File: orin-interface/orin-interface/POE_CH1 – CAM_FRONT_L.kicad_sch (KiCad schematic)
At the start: 1 part, among them J2 653108124022

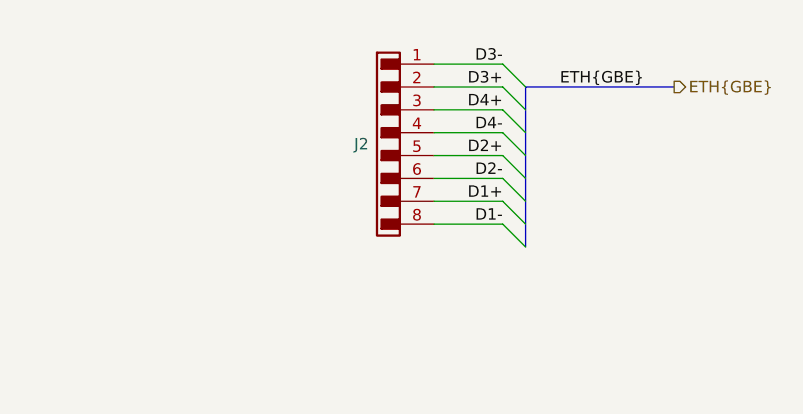
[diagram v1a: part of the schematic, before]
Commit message: orin-interface: add ETH connector sheets and Mate-connectors footprint lib; update orin-bob
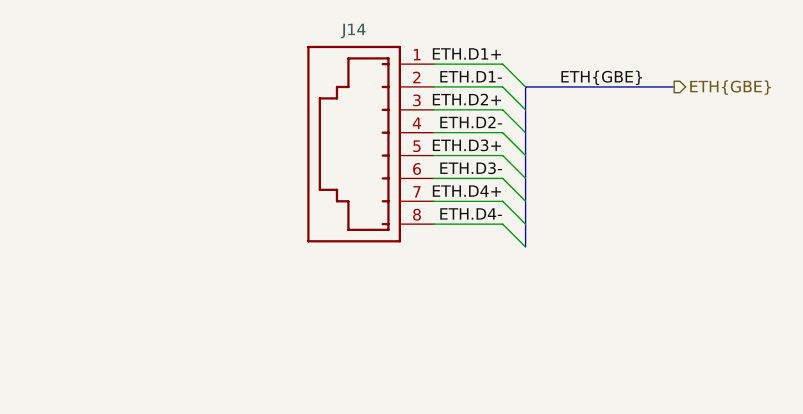
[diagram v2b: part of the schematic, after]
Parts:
- removed J2: 653108124022, Connector_SMD_Wurth:J_Wurth_WR-WTB_653108124022, symbol Wurth_WR-WTB:653108124022
- added J14: 634008138121, 615008138021:J_Wurth_WR-MJ_634008138121, symbol WR-MJ:634008138121
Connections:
- new net ETH.D1+: J14.1
- new net ETH.D1-: J14.2
- new net ETH.D2+: J14.3
- new net ETH.D2-: J14.4
- new net ETH.D3+: J14.5
- new net ETH.D3-: J14.6
- new net ETH.D4+: J14.7
- new net ETH.D4-: J14.8
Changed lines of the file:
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@@
 	(wire
 		(pts
-			(xy 172.72 99.06) (xy 165.1 99.06)
+			(xy 165.1 106.68) (xy 172.72 106.68)
 		)
 		(stroke
@@
 	(wire
 		(pts
-			(xy 172.72 96.52) (xy 165.1 96.52)
+			(xy 165.1 93.98) (xy 172.72 93.98)
 		)
 		(stroke
@@
 		)
 	)
-	(wire
+	(bus
 		(pts
-			(xy 172.72 104.14) (xy 165.1 104.14)
+			(xy 175.26 91.44) (xy 175.26 109.22)
 		)
 		(stroke
@@
 		)
 	)
-	(bus
+	(wire
 		(pts
-			(xy 175.26 91.44) (xy 175.26 109.22)
+			(xy 165.1 96.52) (xy 172.72 96.52)
 		)
 		(stroke
@@
 	(wire
 		(pts
-			(xy 172.72 88.9) (xy 165.1 88.9)
+			(xy 165.1 101.6) (xy 172.72 101.6)
 		)
 		(stroke
@@
 	(wire
 		(pts
-			(xy 172.72 91.44) (xy 165.1 91.44)
+			(xy 165.1 104.14) (xy 172.72 104.14)
 		)
 		(stroke
@@
 	(wire
 		(pts
-			(xy 172.72 101.6) (xy 165.1 101.6)
+			(xy 165.1 99.06) (xy 172.72 99.06)
 		)
 		(stroke
@@
 	(wire
 		(pts
-			(xy 172.72 106.68) (xy 165.1 106.68)
+			(xy 165.1 91.44) (xy 172.72 91.44)
 		)
 		(stroke
@@
 	(wire
 		(pts
-			(xy 172.72 93.98) (xy 165.1 93.98)
+			(xy 165.1 88.9) (xy 172.72 88.9)
 		)
 		(stroke
@@
 		)
 	)
-	(label "D3+"
-		(at 172.72 91.44 180)
+	(label "ETH.D3+"
+		(at 172.72 99.06 180)
 		(effects
 			(font
@@
 		)
 	)
-	(label "D2+"
-		(at 172.72 99.06 180)
+	(label "ETH.D2+"
+		(at 172.72 93.98 180)
 		(effects
 			(font
@@
 		)
 	)
-	(label "D3-"
-		(at 172.72 88.9 180)
+	(label "ETH.D3-"
+		(at 172.72 101.6 180)
 		(effects
 			(font
@@
 		)
 	)
-	(label "D4-"
-		(at 172.72 96.52 180)
+	(label "ETH.D4-"
+		(at 172.72 106.68 180)
 		(effects
 			(font
@@
 		)
 	)
-	(label "D1+"
-		(at 172.72 104.14 180)
+	(label "ETH.D1+"
+		(at 172.72 88.9 180)
 		(effects
 			(font
@@
 		)
 	)
-	(label "D2-"
-		(at 172.72 101.6 180)
+	(label "ETH.D2-"
+		(at 172.72 96.52 180)
 		(effects
 			(font
@@
 		)
 	)
-	(label "D1-"
-		(at 172.72 106.68 180)
+	(label "ETH.D1-"
+		(at 172.72 91.44 180)
 		(effects
 			(font
@@
 		)
 	)
-	(label "D4+"
-		(at 172.72 93.98 180)
+	(label "ETH.D4+"
+		(at 172.72 104.14 180)
 		(effects
 			(font
@@
 	)
 	(symbol
-		(lib_id "Wurth_WR-WTB:653108124022")
-		(at 160.02 97.79 90)
-		(mirror x)
+		(lib_id "WR-MJ:634008138121")
+		(at 156.21 96.52 90)
 		(unit 1)
 		(body_style 1)
@@
 		(in_pos_files yes)
 		(dnp no)
-		(property "Reference" "J2"
-			(at 156.21 97.79 90)
+		(fields_autoplaced yes)
+		(property "Reference" "J14"
+			(at 156.21 85.09 90)
 			(show_name no)
 			(do_not_autoplace no)
@@
 					(size 1.27 1.27)
 				)
-				(justify right)
 			)
 		)
-		(property "Value" "653108124022"
-			(at 172.72 97.79 0)
+		(property "Value" "634008138121"
+			(at 172.72 96.52 0)
 			(hide yes)
 			(show_name no)
@@
 			)
 		)
-		(property "Footprint" "Connector_SMD_Wurth:J_Wurth_WR-WTB_653108124022"
-			(at 152.4 97.79 0)
+		(property "Footprint" "615008138021:J_Wurth_WR-MJ_634008138121"
+			(at 143.51 96.52 0)
 			(hide yes)
 			(show_name no)
@@
 			)
 		)
-		(property "Datasheet" "https://www.we-online.com/en/components/products/datasheet/653108124022?ki"
-			(at 142.24 143.51 0)
+		(property "Datasheet" "https://www.we-online.com/en/components/products/datasheet/634008138121?ki"
+			(at 148.59 33.02 0)
 			(hide yes)
 			(show_name no)
@@
 			)
 		)
-		(property "Description" "1.25 mm SMT Male Vertical Shrouded Header"
-			(at 160.02 97.79 0)
+		(property "Description" "Modular Jack SMT Vertical Plastic 8P8C"
+			(at 156.21 96.52 0)
 			(hide yes)
 			(show_name no)
@@
 		)
 		(property "Manufacturer" "Wurth Elektronik"
-			(at 144.78 143.51 0)
+			(at 151.13 33.02 0)
 			(hide yes)
 			(show_name no)
@@
 		)
 		(property "Manufacturer URL" "https://www.we-online.com"
-			(at 147.32 143.51 0)
-			(hide yes)
-			(show_name no)
-			(do_not_autoplace no)
-			(effects
-				(font
-					(size 1.27 1.27)
-				)
-			)
-		)
-		(property "Series" "WR-WTB"
-			(at 149.86 143.51 0)
-			(hide yes)
-			(show_name no)
-			(do_not_autoplace no)
-			(effects
-				(font
-					(size 1.27 1.27)
-				)
-			)
-		)
-		(property "Pins (pcs)" "8"
-			(at 152.4 143.51 0)
+			(at 153.67 33.02 0)
 			(hide yes)
 			(show_name no)
@@
 			)
 		)
-		(property "Pitch (mm)" "1.25"
-			(at 154.94 143.51 0)
+		(property "Series" "WR-MJ"
+			(at 156.21 33.02 0)
 			(hide yes)
 			(show_name no)
@@
 			)
 		)
-		(property "Gender" "Male"
-			(at 157.48 143.51 0)
+		(property "xPxC" "8P8C"
+			(at 158.75 33.02 0)
 			(hide yes)
 			(show_name no)
@@
 			)
 		)
-		(property "Type" "Vertical"
-			(at 160.02 143.51 0)
+		(property "EMI" "No"
+			(at 161.29 33.02 0)
 			(hide yes)
 			(show_name no)
@@
 			)
 		)
-		(property "Mounting Technology" "SMT"
-			(at 162.56 143.51 0)
+		(property "Mount" "SMT"
+			(at 163.83 33.02 0)
 			(hide yes)
 			(show_name no)
@@
 			)
 		)
-		(property "IR (A)" "1"
-			(at 165.1 143.51 0)
-			(hide yes)
-			(show_name no)
-			(do_not_autoplace no)
-			(effects
-				(font
-					(size 1.27 1.27)
-				)
-			)
-		)
-		(property "Working Voltage (V (AC))" "125"
-			(at 167.64 143.51 0)
-			(hide yes)
-			(show_name no)
-			(do_not_autoplace no)
-			(effects
-				(font
-					(size 1.27 1.27)
-				)
-			)
-		)
-		(property "PCB/Cable/Panel" "PCB"
-			(at 170.18 143.51 0)
-			(hide yes)
-			(show_name no)
-			(do_not_autoplace no)
-			(effects
-				(font
-					(size 1.27 1.27)
-				)
-			)
-		)
-		(property "Contact Resistance (mohm)" "20"
-			(at 172.72 143.51 0)
-			(hide yes)
-			(show_name no)
-			(do_not_autoplace no)
-			(effects
-				(font
-					(size 1.27 1.27)
-				)
-			)
-		)
-		(property "Tol. R" "max."
-			(at 175.26 143.51 0)
-			(hide yes)
-			(show_name no)
-			(do_not_autoplace no)
-			(effects
-				(font
-					(size 1.27 1.27)
-				)
-			)
-		)
-		(property "L (mm)" "14.75"
-			(at 177.8 143.51 0)
+		(property "Application System" "CAT 3"
+			(at 166.37 33.02 0)
 			(hide yes)
 			(show_name no)
@@
 		(pin "3"
 		)
-		(pin "4"
+		(pin "1"
 		)
 		(pin "2"
 		)
-		(pin "5"
+		(pin "4"
 		)
-		(pin "6"
+		(pin "8"
 		)
-		(pin "1"
+		(pin "6"
 		)
-		(pin "8"
+		(pin "5"
 		)
 		(pin "7"
@@
 			(project "orin-interface"
 				(path "/18aef7c7-2f0e-4a2c-9e5d-7b655e80b6a3/25e0c24f-6778-4b98-8756-5687bd49895d"
-					(reference "J2")
+					(reference "J14")
 					(unit 1)
 				)
 				(path "/18aef7c7-2f0e-4a2c-9e5d-7b655e80b6a3/510789d6-7dad-455b-9ae1-5c404d31a377"
-					(reference "J5")
+					(reference "J17")
 					(unit 1)
 				)
 				(path "/18aef7c7-2f0e-4a2c-9e5d-7b655e80b6a3/8c4b4be0-2998-432c-8cd0-24d3943584e4"
-					(reference "J3")
+					(reference "J15")
 					(unit 1)
 				)
 				(path "/18aef7c7-2f0e-4a2c-9e5d-7b655e80b6a3/b5cdc6e0-2ea3-411d-a845-6945aa78fc6c"
-					(reference "J4")
+					(reference "J16")
 					(unit 1)
 				)
